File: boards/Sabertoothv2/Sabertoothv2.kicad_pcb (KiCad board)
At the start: 2 copper layers, 48.3 x 48.3 mm, 26 parts, among them J1 Screw_Terminal_01x04, J2 Screw_Terminal_01x04, Q1 NMOS, Q2 NMOS, Q3 NMOS, Q4 NMOS, U1 LM2104, U2 LM2104, U3 74LVC1GU04DRL

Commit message: edited small stuff
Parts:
- added J3: Conn_01x04_Pin, Connector_PinHeader_2.54mm:PinHeader_1x04_P2.54mm_Vertical, F.Cu at (68.6, 64.4)
- added J4: Conn_01x04_Pin, Connector_PinHeader_2.54mm:PinHeader_1x04_P2.54mm_Vertical, F.Cu at (68.6, 69.1)
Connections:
- Q1 pad 5: (no net) -> VIN+12
- Q2 pad 5: (no net) -> LOAD1
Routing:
- net GND: track 11.0 -> 57.1 mm, vias 2 -> 11
- net PWM: track 42.9 -> 88.0 mm
- net SELECT: track 49.6 -> 91.9 mm, vias 2 -> 4
- net LOAD1: track 57.4 -> 91.9 mm
- net HOA: track 24.9 -> 56.2 mm, vias 0 -> 1
- net VIN+12: track 112.5 -> 143.7 mm, vias 0 -> 1
- net LOA: track 30.0 -> 52.5 mm
- net LOAD2: track 72.3 -> 85.6 mm
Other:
- board text added: "HOA"
- board text added: "IRIS-XIV SAH Ver.2 Rev.B"
- board text added: "LOA"
- board text removed: "IRIS-XIV SAH Ver.2 Rev.A"

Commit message: a
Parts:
- moved CGVDD2 12.9 mm to (53.7, 48.3), turned to 180 degrees
- moved CGVDD1 9.50 mm to (44.5, 37.7), turned to -90 degrees
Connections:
- J4 pad 3: LOA -> LOA1
- J4 pad 4: HOA -> HOA1
- Q1 pad 2: HOA -> HOA1
- Q1 pad 5: VIN+12 -> (no net)
- Q2 pad 2: LOA -> LOA1
- Q2 pad 5: LOAD1 -> (no net)
- Q3 pad 2: HOA -> HOA2
- Q3 pad 5: VIN+12 -> (no net)
- Q4 pad 2: LOA -> LOA2
- Q4 pad 5: LOAD2 -> (no net)
- RGATE1 pad 2: HOA -> HOA1
- RGATE2 pad 2: LOA -> LOA1
- RGATE3 pad 2: HOA -> HOA2
- RGATE4 pad 2: LOA -> LOA2
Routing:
- net LOA1: track 0.00 -> 58.1 mm, vias 0 -> 2
- net HOA: track 56.2 -> 0.00 mm, vias 1 -> 0
- net GND: track 57.1 -> 1.41 mm, vias 11 -> 1
- net LOA: track 52.5 -> 0.00 mm, vias 4 -> 0
- net LOAD1: track 91.9 -> 40.2 mm
- net LOAD2: track 85.6 -> 42.6 mm
- net VIN+12: track 143.7 -> 111.7 mm, vias 1 -> 0
- net LOA2: track 0.00 -> 15.5 mm, vias 0 -> 2
- net HOA2: track 0.00 -> 13.0 mm
- net SELECT: track 91.9 -> 92.9 mm
- removed copper zone on F.Cu, net GND

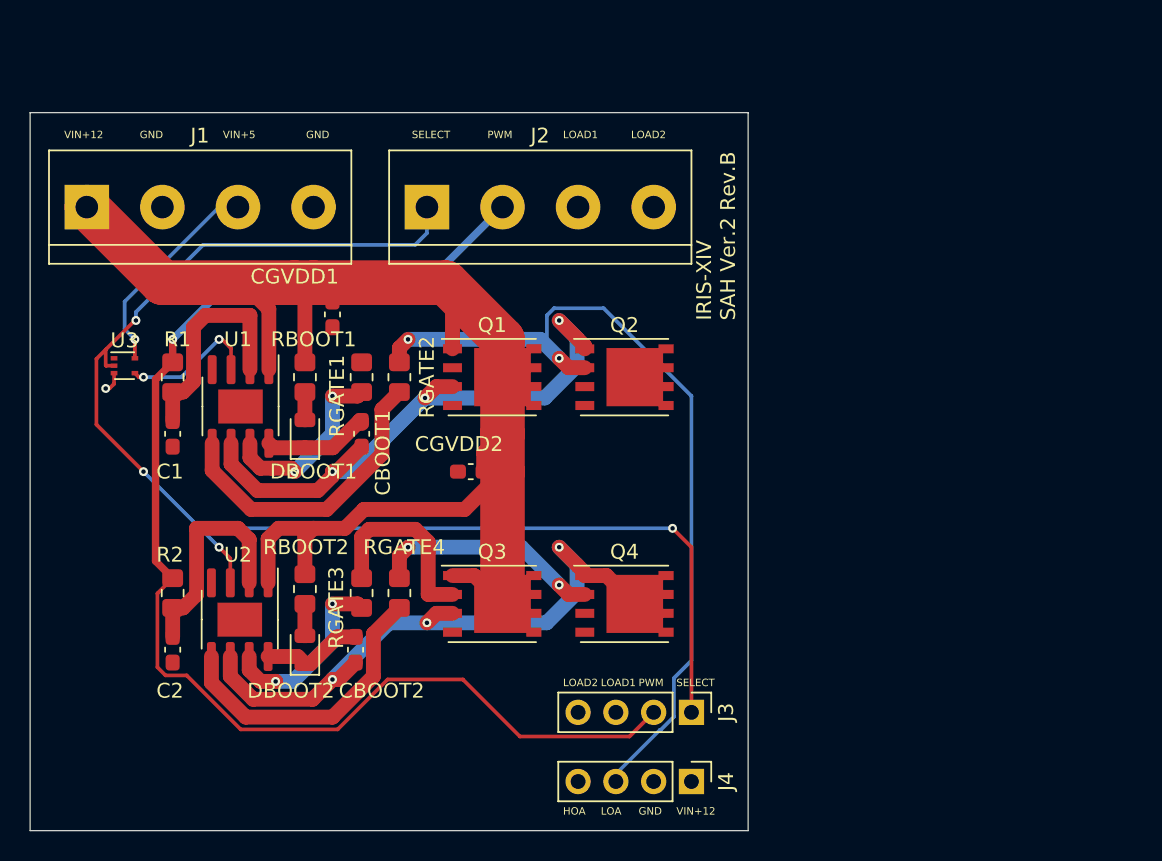
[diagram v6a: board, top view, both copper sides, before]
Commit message: right mosfets
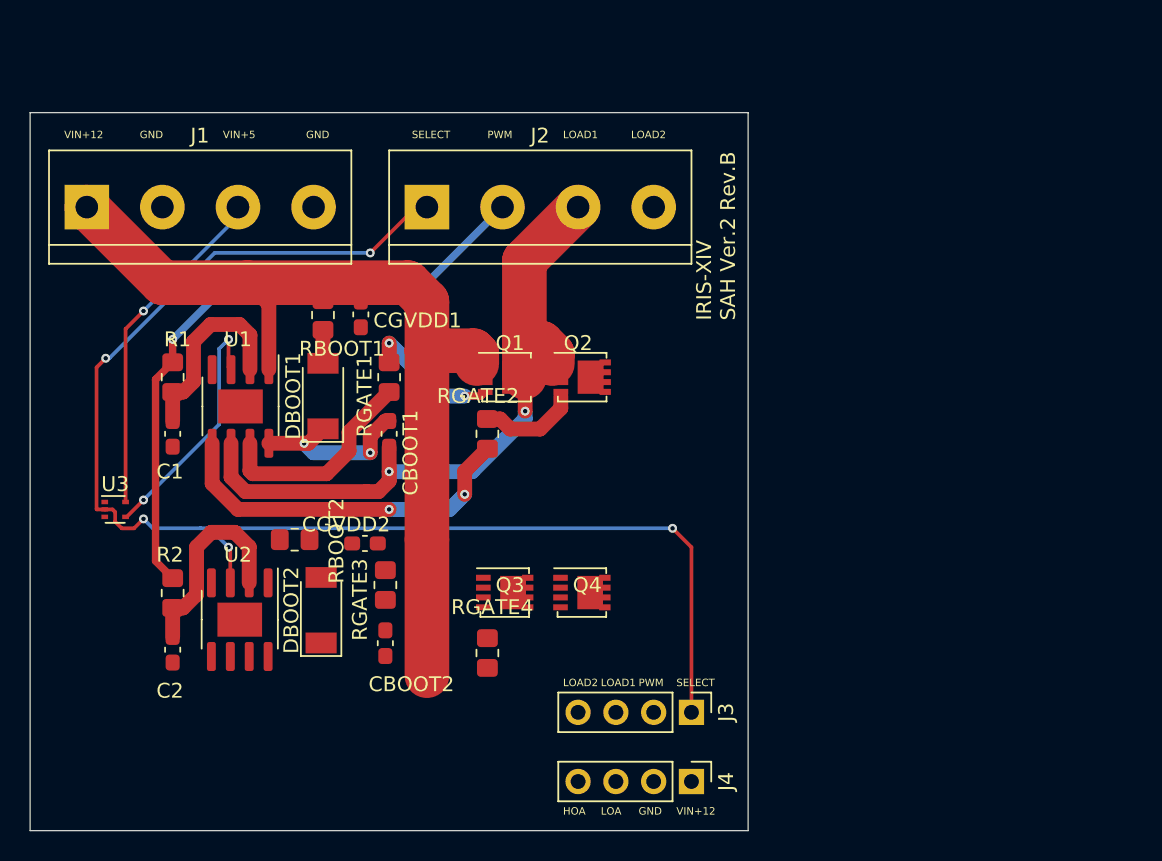
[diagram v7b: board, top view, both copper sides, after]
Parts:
- DBOOT1, DBOOT2: footprint Diode_SMD:D_0805_2012Metric -> Diode_SMD:D_SOD-128
- Q1, Q2, Q3, Q4: footprint Package_SO:PowerPAK_SO-8_Single -> mosfet:PPAK1212-8Custom
- moved U3 9.68 mm to (29.8, 50.8)
- moved CGVDD2 8.59 mm to (46.6, 53.1)
- moved RGATE4 7.16 mm to (54.9, 60.5)
- moved RGATE2 7.04 mm to (54.9, 45.7)
- moved RBOOT1 4.35 mm to (43.8, 37.7)
- moved RBOOT2 3.39 mm to (41.9, 52.8), turned to 180 degrees
- moved DBOOT2 2.87 mm to (43.7, 57.6)
- moved DBOOT1 2.82 mm to (43.8, 43.2)
- moved Q4 2.62 mm to (61.6, 56.4)
- moved Q2 2.48 mm to (61.6, 41.9)
- moved CBOOT2 2.05 mm to (48.0, 59.8)
- moved CGVDD1 1.90 mm to (46.4, 37.7)
- moved CBOOT1 1.85 mm to (48.3, 45.7)
- moved RGATE1 1.85 mm to (48.3, 41.9)
- moved RGATE3 1.68 mm to (48.0, 55.9)
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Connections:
- J1 pad 4: GND -> LGND
- U3 pad 3: GND -> LGND
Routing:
- net LOA1: track 58.1 -> 6.60 mm, vias 2 -> 0
- net VIN+12: track 111.7 -> 61.2 mm
- net PWM: track 88.0 -> 42.9 mm
- net LOAD2: track 42.6 -> 0.00 mm, vias 3 -> 0
- net Net-(U2-GL): track 20.1 -> 0.00 mm
- net LOA2: track 15.5 -> 0.00 mm, vias 2 -> 0
- net HOA2: track 13.0 -> 0.00 mm
- net Net-(U2-GH): track 12.6 -> 0.00 mm, vias 2 -> 0
- net HOA1: track 0.00 -> 9.33 mm, vias 0 -> 2
- net VIN+5: track 14.3 -> 22.9 mm
- net Net-(U1-SD'): track 9.31 -> 16.9 mm
- net Net-(DBOOT2-K): track 6.82 -> 0.00 mm
- net LOAD1: track 40.2 -> 45.1 mm, vias 3 -> 2
- net Net-(DBOOT1-K): track 7.28 -> 11.6 mm, vias 0 -> 2
- net Net-(U1-GL): track 20.5 -> 24.5 mm, vias 0 -> 2
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
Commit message: new pcb design done
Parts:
- C1, C2, CBOOT1, CBOOT2, CGVDD1, CGVDD2: footprint Capacitor_SMD:C_0603_1608Metric_Pad1.08x0.95mm_HandSolder -> Capacitor_SMD:C_0805_2012Metric_Pad1.18x1.45mm_HandSolder
- moved CGVDD2 1.67 mm to (48.3, 52.7)
- moved RBOOT2 1.54 mm to (43.5, 52.8)
- moved RGATE4 1.14 mm to (54.9, 61.6)
- moved C1 0.86 mm to (33.0, 46.2)
- moved C2 0.73 mm to (33.0, 60.5)
- moved R1 0.69 mm to (33.0, 41.9)
- moved R2 0.69 mm to (33.0, 56.4)
- moved RGATE2 0.27 mm to (54.9, 46.0)
- moved DBOOT2 0.05 mm to (43.7, 57.6)
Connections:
- J4 pad 1: VIN+12 -> LOA1
- J4 pad 2: GND -> HOA1
- J4 pad 3: LOA1 -> LOA2
- J4 pad 4: HOA1 -> HOA2
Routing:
- net LOAD2: track 0.00 -> 72.2 mm
- net PWM: track 42.9 -> 86.7 mm
- net HOA1: track 9.33 -> 46.6 mm
- net LOA1: track 6.60 -> 37.7 mm, vias 0 -> 1
- net LGND: track 0.00 -> 30.5 mm, vias 0 -> 1
- net LOAD1: track 45.1 -> 72.1 mm
- net HOA2: track 0.00 -> 23.0 mm, vias 0 -> 1
- net Net-(U2-GL): track 0.00 -> 22.9 mm
- net LOA2: track 0.00 -> 18.1 mm, vias 0 -> 1
- net Net-(U2-GH): track 0.00 -> 15.1 mm
- net Net-(DBOOT2-K): track 0.00 -> 11.1 mm, vias 0 -> 2
- net VIN+12: track 61.2 -> 71.6 mm, vias 0 -> 6
- net Net-(DBOOT2-A): track 0.00 -> 3.07 mm
- net Net-(DBOOT1-K): track 11.6 -> 14.2 mm
- net Net-(U1-IN): track 13.2 -> 14.7 mm
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- added copper zone on B.Cu, net GND
- added copper zone on F.Cu, net GND
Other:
- board text added: "HOA1"
- board text added: "HOA2"
- board text added: "LOA1"
- board text added: "LOA2"
- board text removed: "HOA"
- board text removed: "LOA"
